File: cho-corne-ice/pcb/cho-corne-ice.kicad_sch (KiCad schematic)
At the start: 92 parts, among them J1 MJ-4PP-9, J2 OLED, J3 MJ-4PP-9, J4 OLED, SW1 SW_PUSH, SW10 SW_PUSH, SW11 SW_PUSH, SW12 SW_PUSH, SW13 SW_PUSH, SW14 SW_PUSH, SW15 SW_PUSH, SW16 SW_PUSH, SW17 SW_PUSH, SW18 SW_PUSH, SW19 SW_PUSH, SW2 SW_PUSH, SW20 SW_PUSH, SW21 SW_PUSH, SW22 SW_PUSH, SW23 SW_PUSH, SW24 SW_PUSH, SW25 SW_PUSH, SW26 SW_PUSH, SW27 SW_PUSH, SW28 SW_PUSH, SW29 SW_PUSH, SW3 SW_PUSH, SW30 SW_PUSH, SW31 SW_PUSH, SW32 SW_PUSH, SW33 SW_PUSH, SW34 SW_PUSH, SW35 SW_PUSH, SW36 SW_PUSH, SW37 SW_PUSH, SW38 SW_PUSH, SW39 SW_PUSH, SW4 SW_PUSH, SW40 SW_PUSH, SW41 SW_PUSH, SW42 SW_PUSH, SW5 SW_PUSH, SW6 SW_PUSH, SW7 SW_PUSH, SW8 SW_PUSH, SW9 SW_PUSH, U1 ProMicro, U2 ProMicro

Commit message: mx -> choc hotswap sockets
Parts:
- SW1, SW10, SW11, SW12, SW13, SW14, SW15, SW16, SW17, SW18, SW19, SW2, SW20, SW22, SW23, SW24, SW25, SW26, SW27, SW28, SW29, SW3, SW30, SW31, SW32, SW33, SW34, SW35, SW36, SW37, SW38, SW39, SW4, SW40, SW41, SW5, SW6, SW7, SW8, SW9: footprint kbd:CherryMX_Hotswap -> kbd:ChocV1_V2_Hotswap
- SW21, SW42: footprint kbd:CherryMX_Hotswap_1.5u -> kbd:ChocV1_V2_Hotswap_1.5u

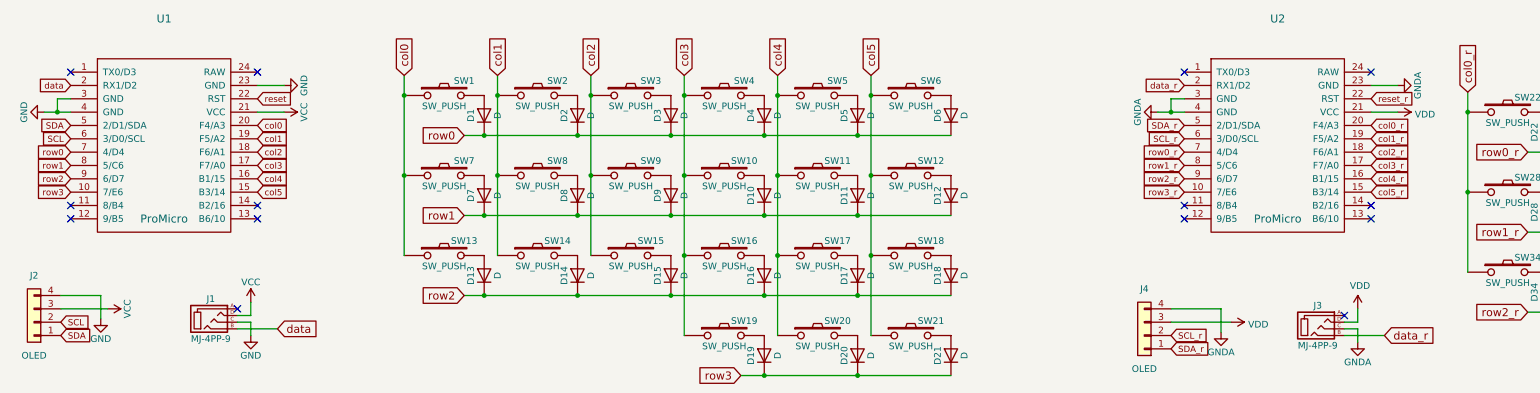
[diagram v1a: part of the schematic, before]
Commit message: add nice!nano, replace Pro Micro footprints with nice!nano
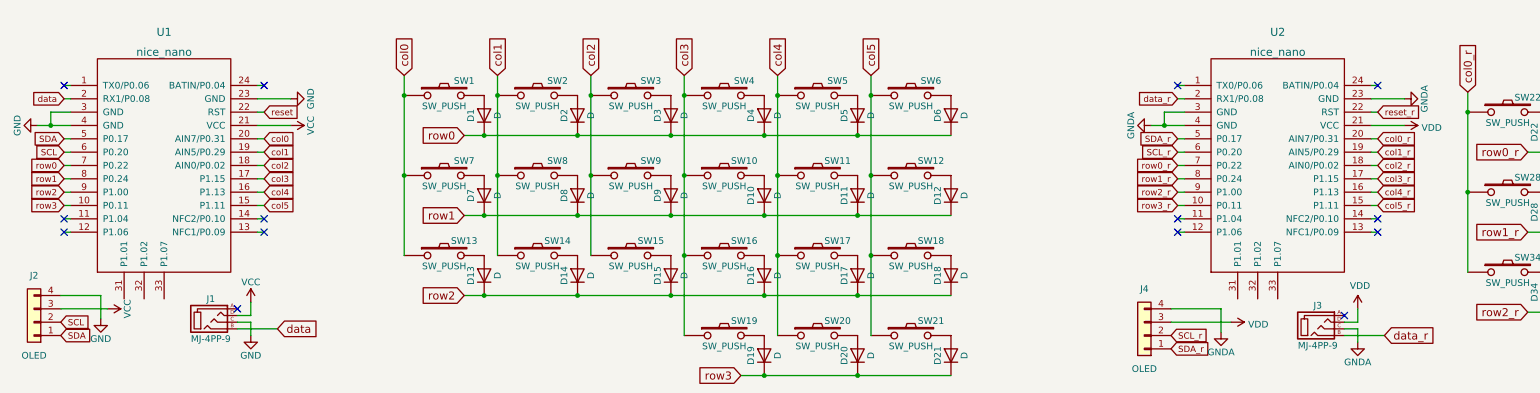
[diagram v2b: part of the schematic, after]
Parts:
- removed U1, U2: ProMicro, kbd:ProMicro_v3, symbol kbd:ProMicro
- added U1, U2: nice_nano, nice-nano-kicad:nice_nano, symbol nice_nano:nice_nano
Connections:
- net GND: now also U1.23 (GND), U1.3 (GND), U1.4 (GND)
- net GNDA: now also U2.23 (GND), U2.3 (GND), U2.4 (GND)
- net SCL: now also U1.6 (P0.20)
- net SCL_r: now also U2.6 (P0.20)
- net SDA: now also U1.5 (P0.17)
- net SDA_r: now also U2.5 (P0.17)
- net VCC: now also U1.21 (VCC)
- net VDD: now also U2.21 (VCC)
- net col0: now also U1.20 (AIN7/P0.31)
- net col0_r: now also U2.20 (AIN7/P0.31)
- net col1: now also U1.19 (AIN5/P0.29)
- net col1_r: now also U2.19 (AIN5/P0.29)
- net col2: now also U1.18 (AIN0/P0.02)
- net col2_r: now also U2.18 (AIN0/P0.02)
- net col3: now also U1.17 (P1.15)
- net col3_r: now also U2.17 (P1.15)
- net col4: now also U1.16 (P1.13)
- net col4_r: now also U2.16 (P1.13)
- net col5: now also U1.15 (P1.11)
- net col5_r: now also U2.15 (P1.11)
- net data: now also U1.2 (RX1/P0.08)
- net data_r: now also U2.2 (RX1/P0.08)
- net reset: now also U1.22 (RST)
- net reset_r: now also U2.22 (RST)
- net row0: now also U1.7 (P0.22)
- net row0_r: now also U2.7 (P0.22)
- net row1: now also U1.8 (P0.24)
- net row1_r: now also U2.8 (P0.24)
- net row2: now also U1.9 (P1.00)
- net row2_r: now also U2.9 (P1.00)
- net row3: now also U1.10 (P0.11)
- net row3_r: now also U2.10 (P0.11)

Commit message: wip
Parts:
- added J1: BAT, Connector_JST:JST_PH_S2B-PH-SM4-TB_1x02-1MP_P2.00mm_Horizontal, symbol Connector_Generic:Conn_01x02
- added PSW1: SW_SPDT, keeblib:switch_SSSS811101, symbol Switch:SW_SPDT
- renumbered J1 to J10
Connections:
- net GND: now also PSW1.2 (B)
- net RAW: now reaches U1.24 (BATIN/P0.04)
- net RAW: now also J1.1 (Pin_1)
- new net: J1.2 (Pin_2), PSW1.1 (A)
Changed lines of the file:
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@@
   (junction (at 144.78 62.865) (diameter 0) (color 0 0 0 0)
   )
-  (no_connect (at 64.77 30.48))
   (no_connect (at 238.76 58.42))
   (no_connect (at 26.67 58.42))
@@
   (no_connect (at 64.77 55.88))
   (no_connect (at 270.51 74.295))
+  (no_connect (at 54.61 92.71))
   (wire (pts (xy 91.44 28.575) (xy 91.44 32.385))
     (stroke (width 0) (type default) (color 0 0 0 0))
@@
     (stroke (width 0) (type default) (color 0 0 0 0))
   )
+  (wire (pts (xy 54.61 87.63) (xy 55.88 87.63))
+    (stroke (width 0) (type default) (color 0 0 0 0))
+  )
   (wire (pts (xy 144.78 32.385) (xy 144.78 47.625))
     (stroke (width 0) (type default) (color 0 0 0 0))
@@
     (stroke (width 0) (type default) (color 0 0 0 0))
   )
+  (wire (pts (xy 64.77 30.48) (xy 63.5 30.48))
+    (stroke (width 0) (type default) (color 0 0 0 0))
+  )
   (wire (pts (xy 276.86 58.42) (xy 275.59 58.42))
     (stroke (width 0) (type default) (color 0 0 0 0))
@@
     (stroke (width 0) (type default) (color 0 0 0 0))
   )
+  (wire (pts (xy 54.61 85.09) (xy 55.88 85.09))
+    (stroke (width 0) (type default) (color 0 0 0 0))
+  )
+  (wire (pts (xy 43.18 90.17) (xy 44.45 90.17))
+    (stroke (width 0) (type default) (color 0 0 0 0))
+  )
   (wire (pts (xy 127 28.575) (xy 127 32.385))
     (stroke (width 0) (type default) (color 0 0 0 0))
@@
     (stroke (width 0) (type default) (color 0 0 0 0))
   )
+  (wire (pts (xy 43.18 91.44) (xy 43.18 90.17))
+    (stroke (width 0) (type default) (color 0 0 0 0))
+  )
   (wire (pts (xy 238.76 50.8) (xy 240.03 50.8))
     (stroke (width 0) (type default) (color 0 0 0 0))
@@
   )
   (wire (pts (xy 309.245 43.18) (xy 327.025 43.18))
-    (stroke (width 0) (type default) (color 0 0 0 0))
-  )
-  (wire (pts (xy 64.77 30.48) (xy 63.5 30.48))
     (stroke (width 0) (type default) (color 0 0 0 0))
   )
@@
     )
   )
+  (global_label "RAW" (shape input) (at 64.77 30.48 0) (fields_autoplaced)
+    (effects (font (size 1.27 1.27)) (justify left))
+    (property "Intersheet References" "${INTERSHEET_REFS}" (id 0) (at 70.9042 30.4006 0)
+      (effects (font (size 1.27 1.27)) (justify left) hide)
+    )
+  )
   (global_label "data_r" (shape input) (at 238.76 33.02 180) (fields_autoplaced)
     (effects (font (size 1.1938 1.1938)) (justify right))
@@
     )
   )
+  (global_label "RAW" (shape input) (at 54.61 85.09 180) (fields_autoplaced)
+    (effects (font (size 1.27 1.27)) (justify right))
+    (property "Intersheet References" "${INTERSHEET_REFS}" (id 0) (at 48.4758 85.0106 0)
+      (effects (font (size 1.27 1.27)) (justify right) hide)
+    )
+  )
   (global_label "col3" (shape input) (at 64.77 48.26 0) (fields_autoplaced)
     (effects (font (size 1.1938 1.1938)) (justify left))
@@
   (symbol (lib_id "kbd:MJ-4PP-9") (at 54.61 74.93 0) (unit 1)
     (in_bom yes) (on_board yes)
-    (property "Reference" "J1" (id 0) (at 54.61 71.12 0))
+    (property "Reference" "J10" (id 0) (at 54.61 71.12 0))
     (property "Value" "MJ-4PP-9" (id 1) (at 54.61 78.74 0))
     (property "Footprint" "kbd:MJ-4PP-9_1side" (id 2) (at 61.595 70.485 0)
@@
     )
     (pin "1")
+  )
+  (symbol (lib_id "power:GND") (at 43.18 91.44 0) (unit 1)
+    (in_bom yes) (on_board yes)
+    (property "Reference" "#PWR0101" (id 0) (at 43.18 97.79 0)
+      (effects (font (size 1.27 1.27)) hide)
+    )
+    (property "Value" "GND" (id 1) (at 43.18 95.25 0))
+    (property "Footprint" "" (id 2) (at 43.18 91.44 0)
+      (effects (font (size 1.27 1.27)) hide)
+    )
+    (property "Datasheet" "" (id 3) (at 43.18 91.44 0)
+      (effects (font (size 1.27 1.27)) hide)
+    )
+    (pin "1")
+  )
+  (symbol (lib_id "Switch:SW_SPDT") (at 49.53 90.17 0) (unit 1)
+    (in_bom yes) (on_board yes)
+    (property "Reference" "PSW1" (id 0) (at 49.53 96.52 0))
+    (property "Value" "SW_SPDT" (id 1) (at 49.53 99.06 0))
+    (property "Footprint" "keeblib:switch_SSSS811101" (id 2) (at 49.53 90.17 0)
+      (effects (font (size 1.27 1.27)) hide)
+    )
+    (property "Datasheet" "~" (id 3) (at 49.53 90.17 0)
+      (effects (font (size 1.27 1.27)) hide)
+    )
+    (pin "1")
+    (pin "2")
+    (pin "3")
   )
   (symbol (lib_id "nice_nano:nice_nano") (at 45.72 44.45 0) (unit 1)
@@
     (pin "9")
   )
+  (symbol (lib_id "Connector_Generic:Conn_01x02") (at 60.96 85.09 0) (unit 1)
+    (in_bom yes) (on_board yes) (fields_autoplaced)
+    (property "Reference" "J1" (id 0) (at 63.5 85.0899 0)
+      (effects (font (size 1.27 1.27)) (justify left))
+    )
+    (property "Value" "BAT" (id 1) (at 63.5 87.6299 0)
+      (effects (font (size 1.27 1.27)) (justify left))
+    )
+    (property "Footprint" "Connector_JST:JST_PH_S2B-PH-SM4-TB_1x02-1MP_P2.00mm_Horizontal" (id 2) (at 60.96 85.09 0)
+      (effects (font (size 1.27 1.27)) hide)
+    )
+    (property "Datasheet" "~" (id 3) (at 60.96 85.09 0)
+      (effects (font (size 1.27 1.27)) hide)
+    )
+    (pin "1")
+    (pin "2")
+  )
   (sheet_instances
     (path "/" (page "1"))
@@
       (reference "#PWR024") (unit 1) (value "GNDA") (footprint "")
     )
+    (path "/7fb44e9f-1c1c-4e5f-9a9c-b8f9fc64faee"
+      (reference "#PWR0101") (unit 1) (value "GND") (footprint "")
+    )
     (path "/00000000-0000-0000-0000-00005a5e2b5b"
       (reference "D1") (unit 1) (value "D") (footprint "kbd:D3_SMD_v2")
@@
       (reference "D42") (unit 1) (value "D") (footprint "kbd:D3_SMD_v2")
     )
-    (path "/00000000-0000-0000-0000-00005acd605d"
-      (reference "J1") (unit 1) (value "MJ-4PP-9") (footprint "kbd:MJ-4PP-9_1side")
+    (path "/fa9e90f3-8244-4c54-8317-e2a50e553f7f"
+      (reference "J1") (unit 1) (value "BAT") (footprint "Connector_JST:JST_PH_S2B-PH-SM4-TB_1x02-1MP_P2.00mm_Horizontal")
     )
     (path "/00000000-0000-0000-0000-00005a91da4b"
@@
       (reference "J4") (unit 1) (value "OLED") (footprint "kbd:OLED_1side")
     )
+    (path "/00000000-0000-0000-0000-00005acd605d"
+      (reference "J10") (unit 1) (value "MJ-4PP-9") (footprint "kbd:MJ-4PP-9_1side")
+    )
+    (path "/c4ae925a-e751-48cc-b685-a4bdffc8b40b"
+      (reference "PSW1") (unit 1) (value "SW_SPDT") (footprint "keeblib:switch_SSSS811101")
+    )
     (path "/00000000-0000-0000-0000-00005a5eb9e2"

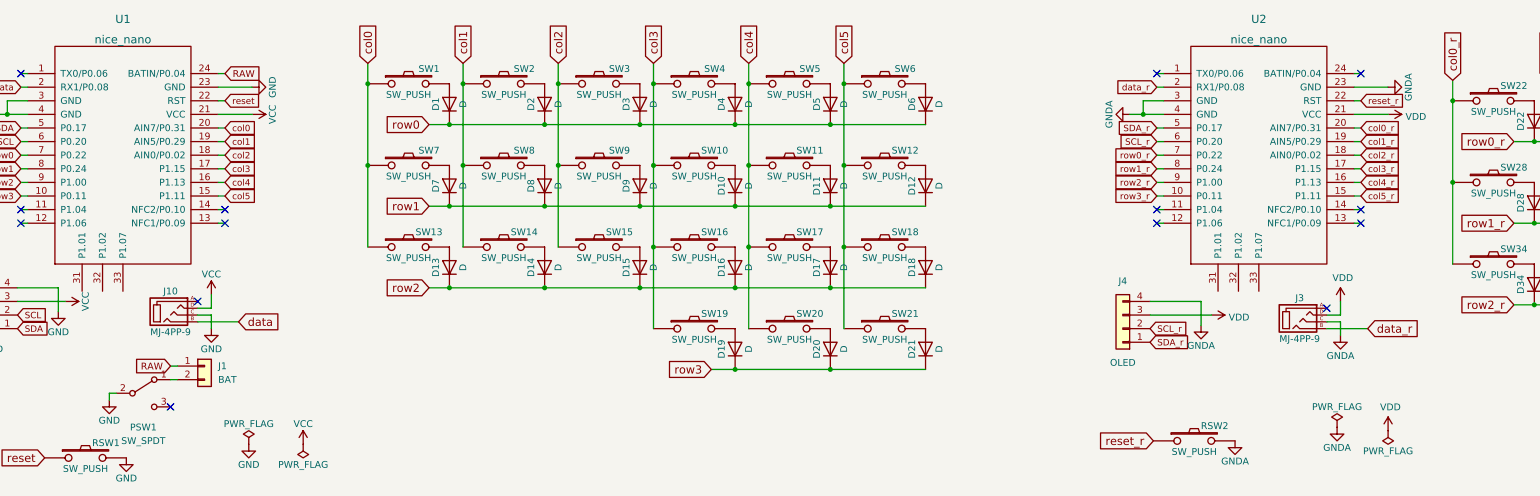
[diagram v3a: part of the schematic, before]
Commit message: complete battery jumper and power switch, clean up nets again
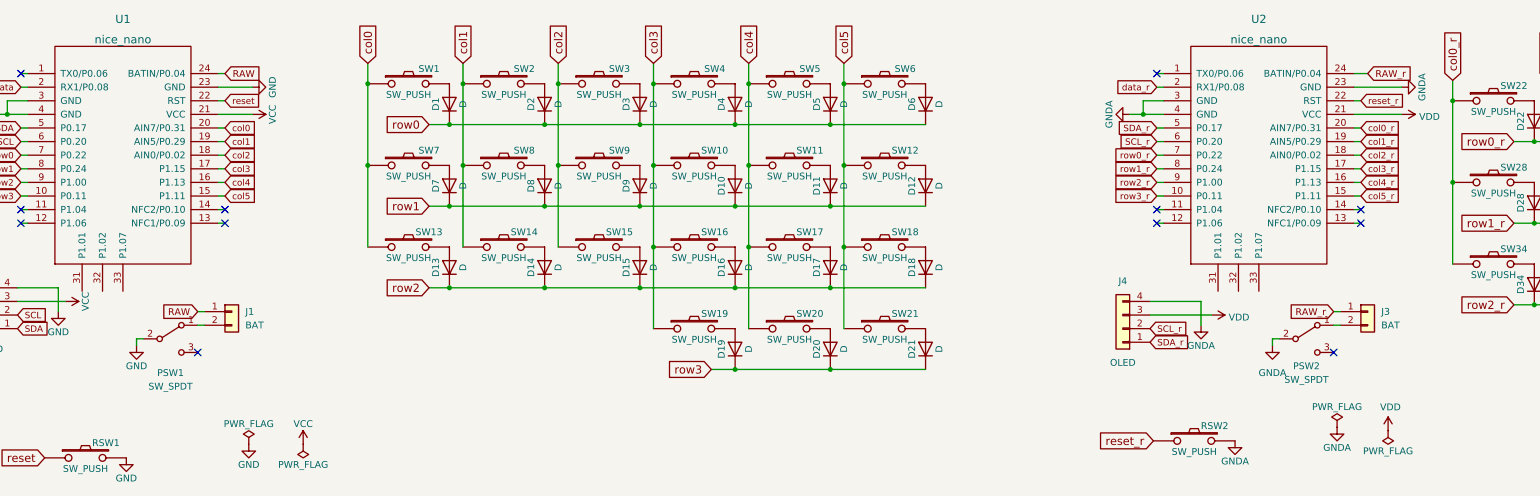
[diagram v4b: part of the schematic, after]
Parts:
- removed J10, J3: MJ-4PP-9, kbd:MJ-4PP-9_1side, symbol kbd:MJ-4PP-9
- added J3: BAT, Connector_JST:JST_PH_S2B-PH-SM4-TB_1x02-1MP_P2.00mm_Horizontal, symbol Connector_Generic:Conn_01x02
- added PSW2: SW_SPDT, keeblib:switch_SSSS811101, symbol Switch:SW_SPDT
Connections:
- net GNDA: now also PSW2.2 (B)
- net RAW_r: now reaches U2.24 (BATIN/P0.04)
- net RAW_r: now also J3.1 (Pin_1)
- new net: J3.2 (Pin_2), PSW2.1 (A)
- no-connect marks 14 -> 12
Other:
- moved on the sheet: J1, PSW1

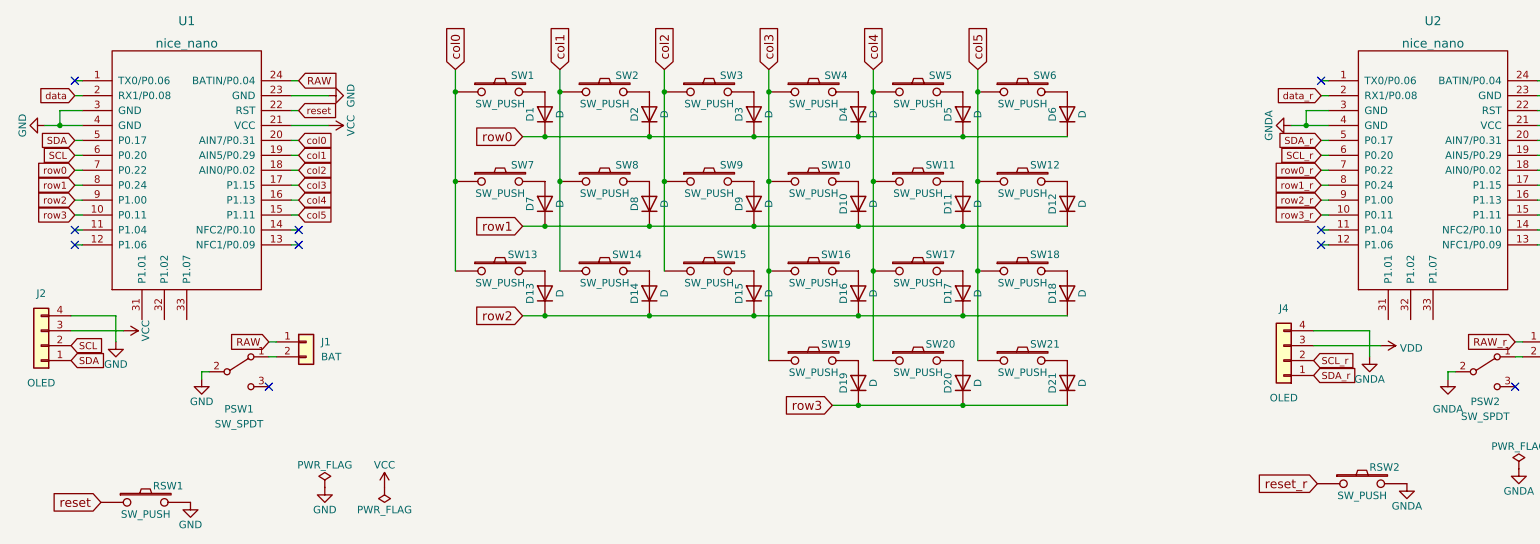
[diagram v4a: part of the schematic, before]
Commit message: finish switches and nice!view
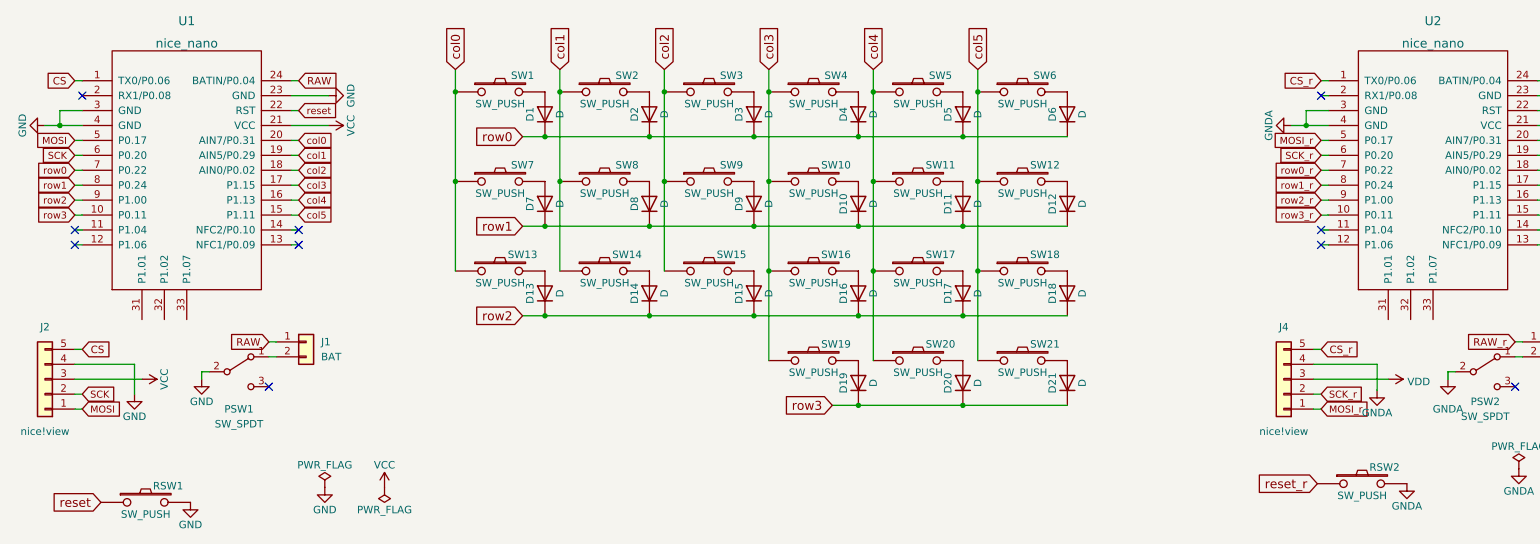
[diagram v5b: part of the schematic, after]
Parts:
- removed J2, J4: OLED, kbd:OLED_1side, symbol Connector_Generic:Conn_01x04
- added J2, J4: nice!view, Connector_PinSocket_2.54mm:PinSocket_1x05_P2.54mm_Vertical, symbol Connector_Generic:Conn_01x05
- RSW1, RSW2: footprint kbd:ResetSW_1side -> keeblib:alps_sksn
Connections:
- net GND: now also J2.4 (Pin_4)
- net GNDA: now also J4.4 (Pin_4)
- net VCC: now also J2.3 (Pin_3)
- net VDD: now also J4.3 (Pin_3)
- net CS: now reaches U1.1 (TX0/P0.06)
- net CS: now also J2.5 (Pin_5)
- net CS_r: now reaches U2.1 (TX0/P0.06)
- net CS_r: now also J4.5 (Pin_5)
- net SCL renamed SCK
- net SCK: now also J2.2 (Pin_2)
- net SCL_r renamed SCK_r
- net SCK_r: now also J4.2 (Pin_2)
- net SDA renamed MOSI
- net MOSI: now also J2.1 (Pin_1)
- net SDA_r renamed MOSI_r
- net MOSI_r: now also J4.1 (Pin_1)
- net data: no longer names the net of U1.2 (RX1/P0.08)
- net data_r: no longer names the net of U2.2 (RX1/P0.08)

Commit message: revert reset switches
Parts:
- RSW1, RSW2: footprint keeblib:alps_sksn -> kbd:ResetSW_1side
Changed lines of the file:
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@@
     (property "Reference" "RSW1" (id 0) (at 42.545 99.441 0))
     (property "Value" "SW_PUSH" (id 1) (at 38.735 104.267 0))
-    (property "Footprint" "keeblib:alps_sksn" (id 2) (at 38.735 102.235 0)
+    (property "Footprint" "kbd:ResetSW_1side" (id 2) (at 38.735 102.235 0)
       (effects (font (size 1.27 1.27)) hide)
     )
@@
     (property "Reference" "RSW2" (id 0) (at 249.555 96.266 0))
     (property "Value" "SW_PUSH" (id 1) (at 245.745 101.092 0))
-    (property "Footprint" "keeblib:alps_sksn" (id 2) (at 245.745 99.06 0)
+    (property "Footprint" "kbd:ResetSW_1side" (id 2) (at 245.745 99.06 0)
       (effects (font (size 1.27 1.27)) hide)
     )
@@
     )
     (path "/00000000-0000-0000-0000-00005a5eb9e2"
-      (reference "RSW1") (unit 1) (value "SW_PUSH") (footprint "keeblib:alps_sksn")
+      (reference "RSW1") (unit 1) (value "SW_PUSH") (footprint "kbd:ResetSW_1side")
     )
     (path "/00000000-0000-0000-0000-00005c25f978"
-      (reference "RSW2") (unit 1) (value "SW_PUSH") (footprint "keeblib:alps_sksn")
+      (reference "RSW2") (unit 1) (value "SW_PUSH") (footprint "kbd:ResetSW_1side")
     )
     (path "/00000000-0000-0000-0000-00005a5e2b19"
